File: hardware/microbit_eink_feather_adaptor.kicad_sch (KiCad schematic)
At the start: 2 parts

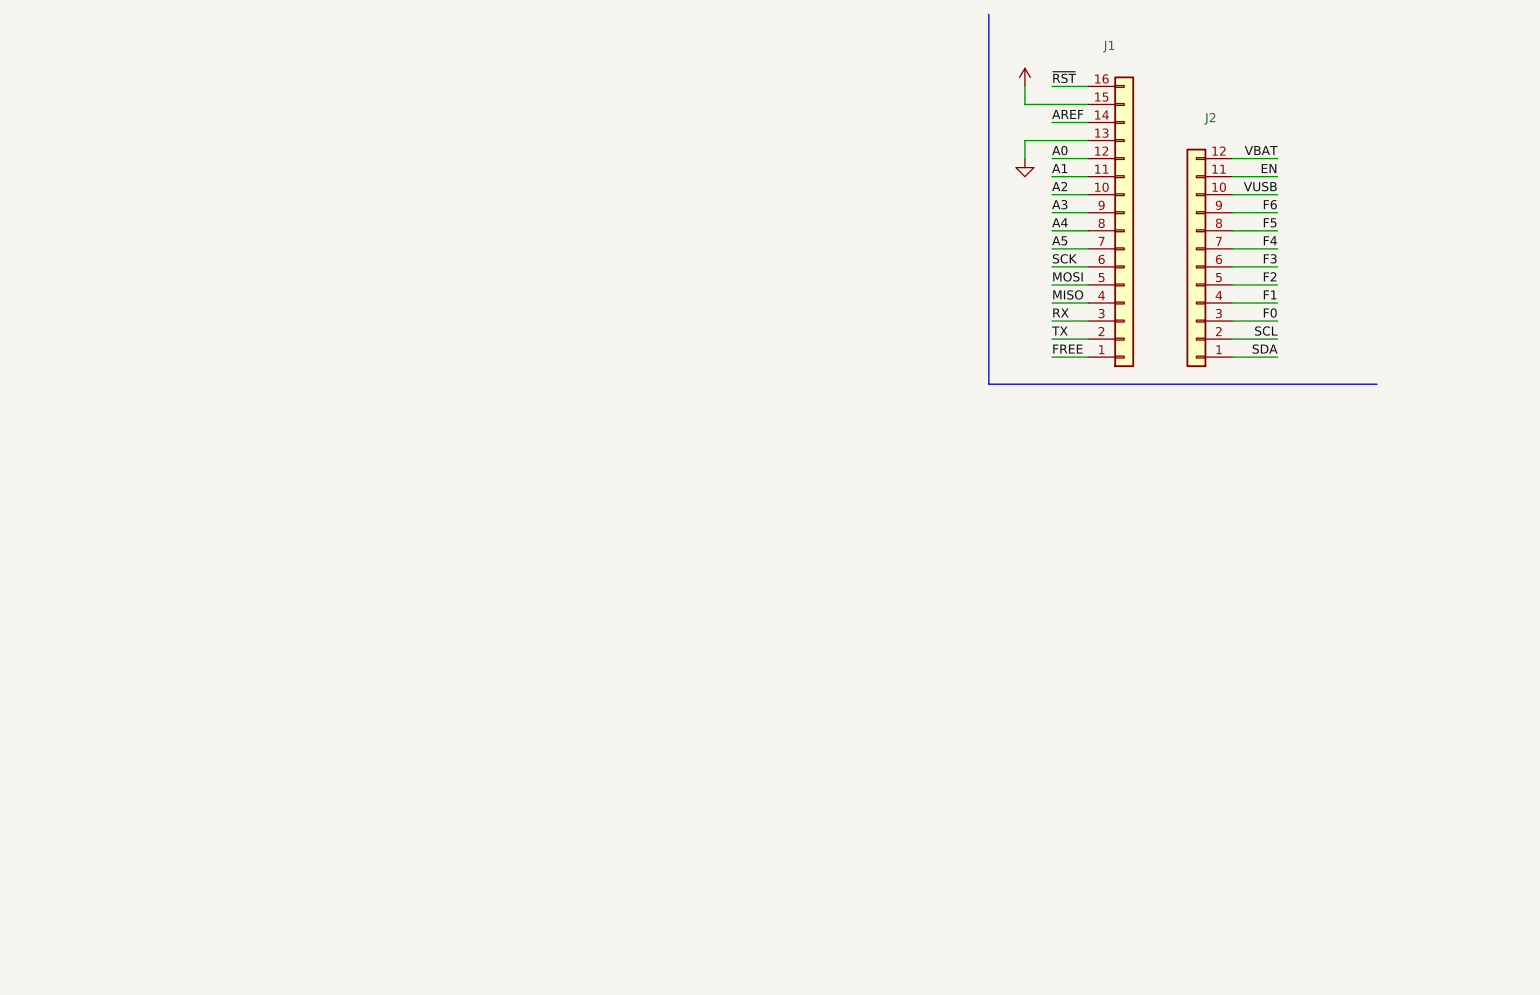
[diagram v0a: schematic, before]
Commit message: Add micro:bit edge connector to project.
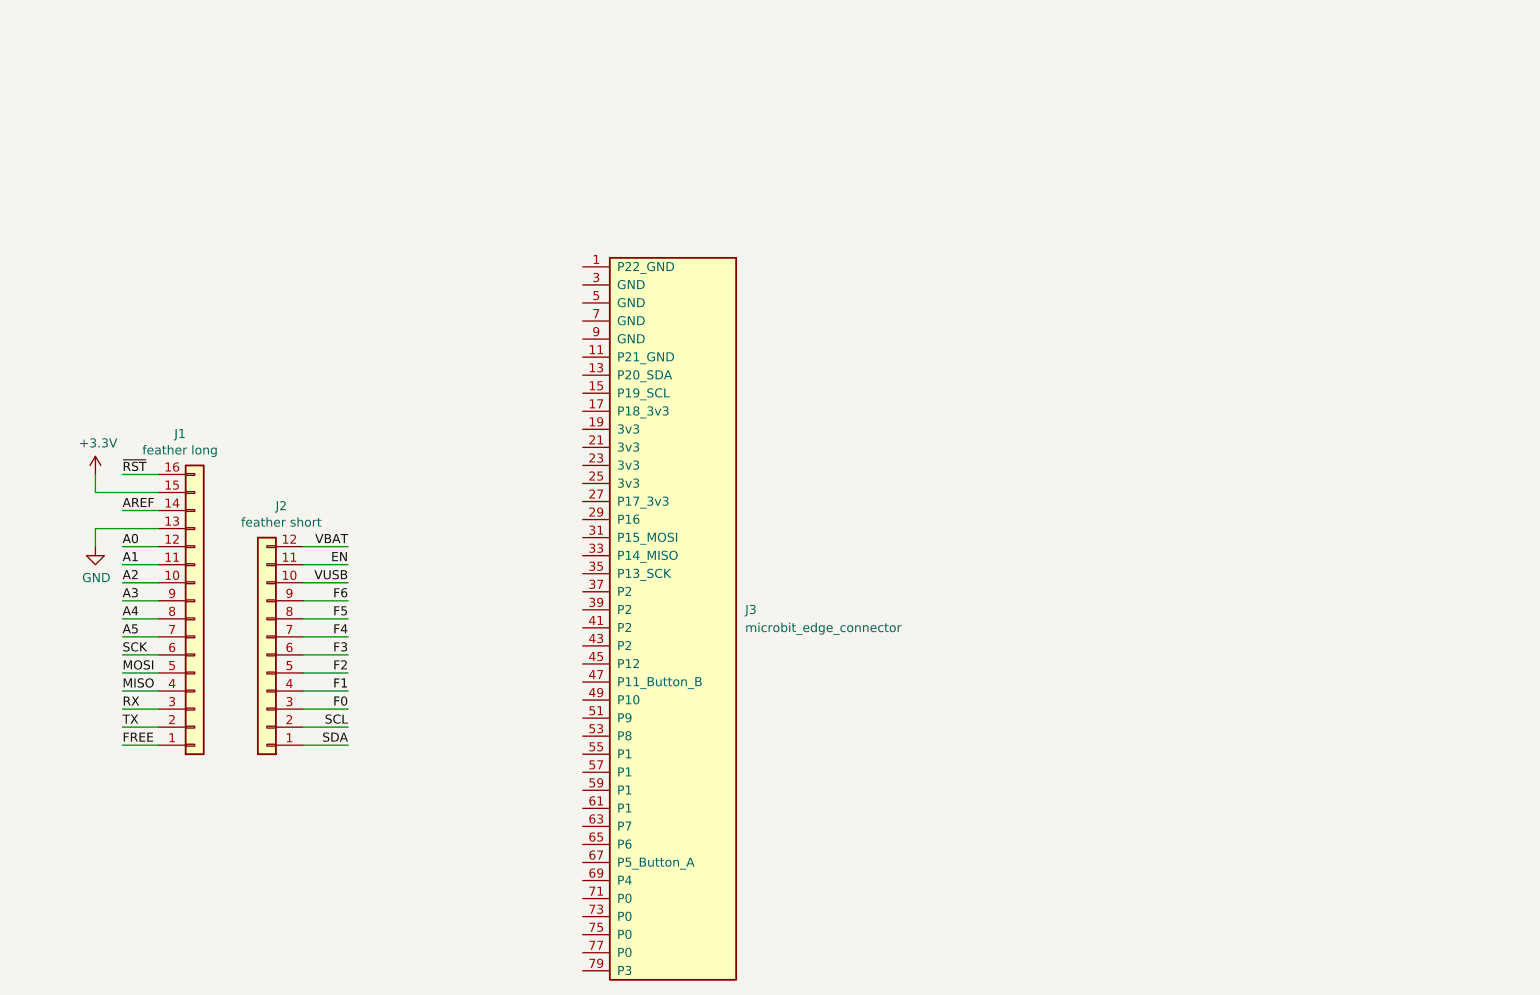
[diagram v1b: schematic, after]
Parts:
- added J3: microbit_edge_connector, symbol lib_microbit_connector:microbit_edge_connector
- J1: value (none) -> feather long; footprint (none) -> Connector_PinHeader_2.54mm:PinHeader_1x16_P2.54mm_Vertical
- J2: value (none) -> feather short; footprint (none) -> Connector_PinHeader_2.54mm:PinHeader_1x12_P2.54mm_Vertical
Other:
- moved on the sheet: J1, J2

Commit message: Increase board size, place edge connector, and route 3V, GND, and SPI pins.
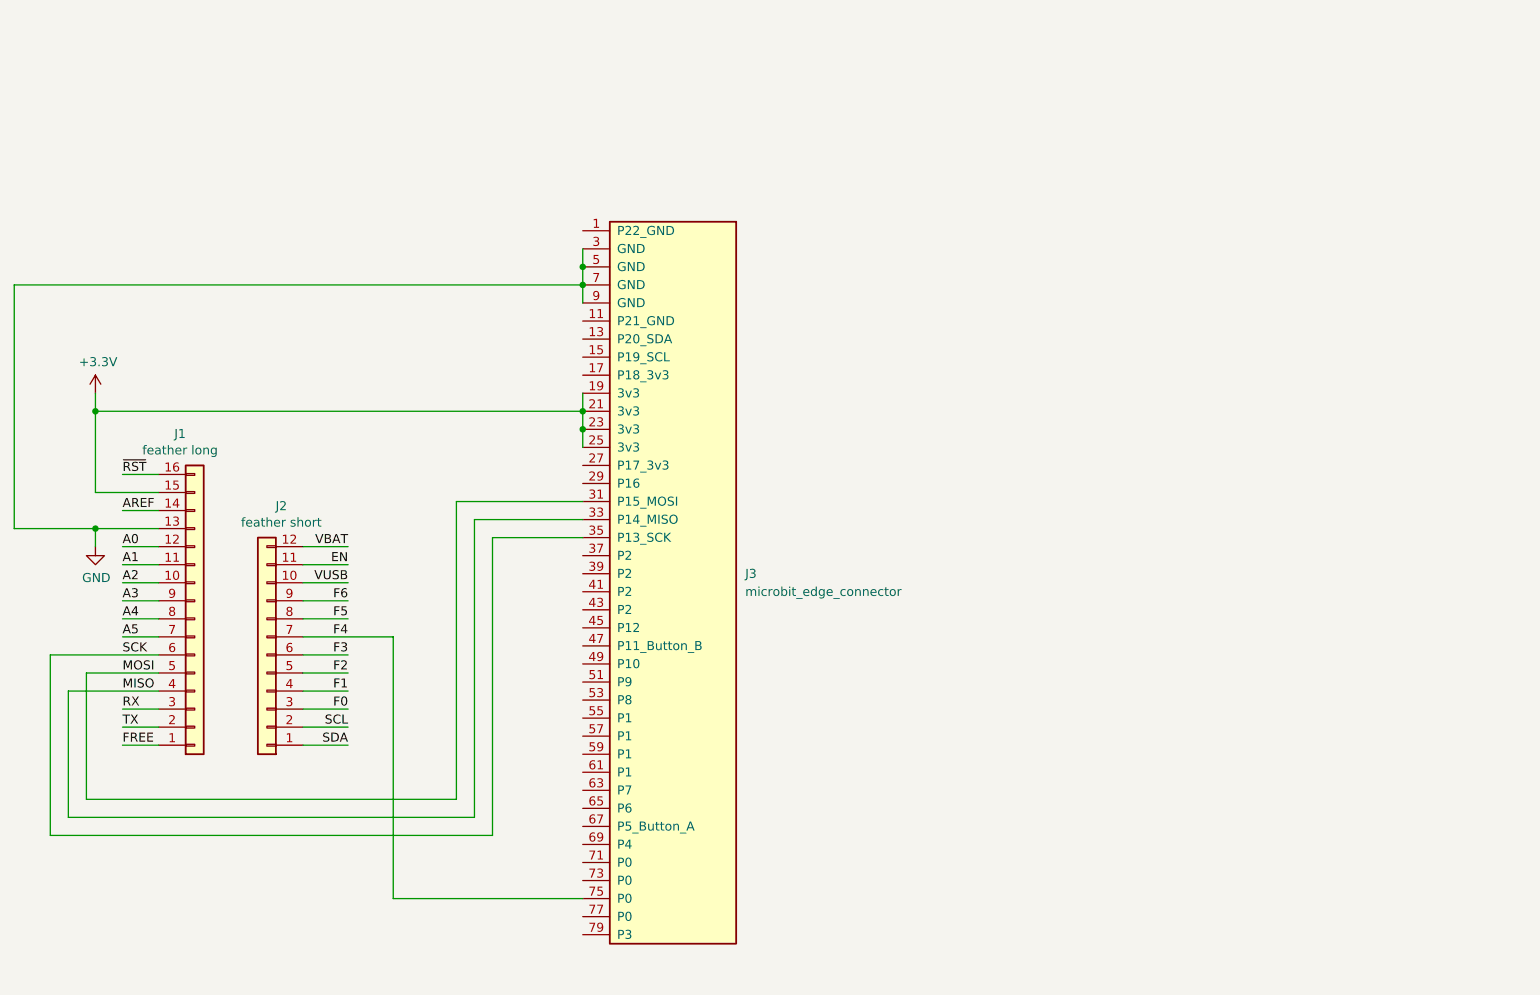
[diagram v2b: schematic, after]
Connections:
- net +3V3: now also J3.19 (3v3), J3.21 (3v3), J3.23 (3v3), J3.25 (3v3)
- net F4: now also J3.75 (P0)
- net GND: now also J3.3 (GND), J3.5 (GND), J3.7 (GND), J3.9 (GND)
- net MISO: now also J3.33 (P14_MISO)
- net MOSI: now also J3.31 (P15_MOSI)
- net SCK: now also J3.35 (P13_SCK)
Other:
- moved on the sheet: J3
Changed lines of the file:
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@@
 (kicad_sch (version 20211123) (generator eeschema)
   (paper "USLetter")
+  (junction (at 154.94 68.58) (diameter 0) (color 0 0 0 0)
+  )
+  (junction (at 154.94 48.26) (diameter 0) (color 0 0 0 0)
+  )
+  (junction (at 154.94 71.12) (diameter 0) (color 0 0 0 0)
+  )
+  (junction (at 154.94 50.8) (diameter 0) (color 0 0 0 0)
+  )
+  (junction (at 86.36 85.09) (diameter 0) (color 0 0 0 0)
+  )
+  (junction (at 86.36 68.58) (diameter 0) (color 0 0 0 0)
+  )
   (wire (pts (xy 90.17 82.55) (xy 95.25 82.55))
     (stroke (width 0) (type default) (color 0 0 0 0))
   )
-  (wire (pts (xy 90.17 102.87) (xy 95.25 102.87))
+  (wire (pts (xy 142.24 86.36) (xy 142.24 128.27))
+    (stroke (width 0) (type default) (color 0 0 0 0))
+  )
+  (wire (pts (xy 139.7 83.82) (xy 139.7 125.73))
+    (stroke (width 0) (type default) (color 0 0 0 0))
+  )
+  (wire (pts (xy 154.94 137.16) (xy 128.27 137.16))
     (stroke (width 0) (type default) (color 0 0 0 0))
   )
@@
     (stroke (width 0) (type default) (color 0 0 0 0))
   )
+  (wire (pts (xy 154.94 71.12) (xy 154.94 73.66))
+    (stroke (width 0) (type default) (color 0 0 0 0))
+  )
+  (wire (pts (xy 154.94 83.82) (xy 139.7 83.82))
+    (stroke (width 0) (type default) (color 0 0 0 0))
+  )
+  (wire (pts (xy 82.55 125.73) (xy 82.55 107.95))
+    (stroke (width 0) (type default) (color 0 0 0 0))
+  )
+  (wire (pts (xy 154.94 81.28) (xy 137.16 81.28))
+    (stroke (width 0) (type default) (color 0 0 0 0))
+  )
+  (wire (pts (xy 154.94 66.04) (xy 154.94 68.58))
+    (stroke (width 0) (type default) (color 0 0 0 0))
+  )
   (wire (pts (xy 115.57 102.87) (xy 121.92 102.87))
     (stroke (width 0) (type default) (color 0 0 0 0))
@@
     (stroke (width 0) (type default) (color 0 0 0 0))
   )
+  (wire (pts (xy 85.09 105.41) (xy 95.25 105.41))
+    (stroke (width 0) (type default) (color 0 0 0 0))
+  )
   (wire (pts (xy 90.17 115.57) (xy 95.25 115.57))
     (stroke (width 0) (type default) (color 0 0 0 0))
   )
+  (wire (pts (xy 86.36 68.58) (xy 154.94 68.58))
+    (stroke (width 0) (type default) (color 0 0 0 0))
+  )
   (wire (pts (xy 115.57 115.57) (xy 121.92 115.57))
     (stroke (width 0) (type default) (color 0 0 0 0))
   )
+  (wire (pts (xy 154.94 68.58) (xy 154.94 71.12))
+    (stroke (width 0) (type default) (color 0 0 0 0))
+  )
   (wire (pts (xy 90.17 113.03) (xy 95.25 113.03))
     (stroke (width 0) (type default) (color 0 0 0 0))
   )
+  (wire (pts (xy 137.16 123.19) (xy 85.09 123.19))
+    (stroke (width 0) (type default) (color 0 0 0 0))
+  )
   (wire (pts (xy 115.57 90.17) (xy 121.92 90.17))
     (stroke (width 0) (type default) (color 0 0 0 0))
@@
     (stroke (width 0) (type default) (color 0 0 0 0))
   )
-  (wire (pts (xy 90.17 105.41) (xy 95.25 105.41))
-    (stroke (width 0) (type default) (color 0 0 0 0))
-  )
   (wire (pts (xy 115.57 97.79) (xy 121.92 97.79))
     (stroke (width 0) (type default) (color 0 0 0 0))
   )
+  (wire (pts (xy 128.27 137.16) (xy 128.27 100.33))
+    (stroke (width 0) (type default) (color 0 0 0 0))
+  )
   (wire (pts (xy 86.36 87.63) (xy 86.36 85.09))
     (stroke (width 0) (type default) (color 0 0 0 0))
@@
     (stroke (width 0) (type default) (color 0 0 0 0))
   )
+  (wire (pts (xy 74.93 85.09) (xy 86.36 85.09))
+    (stroke (width 0) (type default) (color 0 0 0 0))
+  )
+  (wire (pts (xy 86.36 68.58) (xy 86.36 80.01))
+    (stroke (width 0) (type default) (color 0 0 0 0))
+  )
   (wire (pts (xy 115.57 113.03) (xy 121.92 113.03))
     (stroke (width 0) (type default) (color 0 0 0 0))
@@
     (stroke (width 0) (type default) (color 0 0 0 0))
   )
-  (wire (pts (xy 90.17 107.95) (xy 95.25 107.95))
+  (wire (pts (xy 82.55 107.95) (xy 95.25 107.95))
     (stroke (width 0) (type default) (color 0 0 0 0))
   )
@@
     (stroke (width 0) (type default) (color 0 0 0 0))
   )
+  (wire (pts (xy 80.01 128.27) (xy 80.01 102.87))
+    (stroke (width 0) (type default) (color 0 0 0 0))
+  )
+  (wire (pts (xy 85.09 123.19) (xy 85.09 105.41))
+    (stroke (width 0) (type default) (color 0 0 0 0))
+  )
+  (wire (pts (xy 142.24 128.27) (xy 80.01 128.27))
+    (stroke (width 0) (type default) (color 0 0 0 0))
+  )
   (wire (pts (xy 90.17 95.25) (xy 95.25 95.25))
     (stroke (width 0) (type default) (color 0 0 0 0))
   )
+  (wire (pts (xy 154.94 45.72) (xy 154.94 48.26))
+    (stroke (width 0) (type default) (color 0 0 0 0))
+  )
+  (wire (pts (xy 74.93 50.8) (xy 74.93 85.09))
+    (stroke (width 0) (type default) (color 0 0 0 0))
+  )
+  (wire (pts (xy 154.94 50.8) (xy 154.94 53.34))
+    (stroke (width 0) (type default) (color 0 0 0 0))
+  )
   (wire (pts (xy 86.36 85.09) (xy 95.25 85.09))
     (stroke (width 0) (type default) (color 0 0 0 0))
@@
     (stroke (width 0) (type default) (color 0 0 0 0))
   )
-  (wire (pts (xy 115.57 100.33) (xy 121.92 100.33))
+  (wire (pts (xy 139.7 125.73) (xy 82.55 125.73))
     (stroke (width 0) (type default) (color 0 0 0 0))
   )
@@
     (stroke (width 0) (type default) (color 0 0 0 0))
   )
-  (wire (pts (xy 86.36 77.47) (xy 86.36 80.01))
+  (wire (pts (xy 86.36 66.04) (xy 86.36 68.58))
+    (stroke (width 0) (type default) (color 0 0 0 0))
+  )
+  (wire (pts (xy 115.57 100.33) (xy 128.27 100.33))
+    (stroke (width 0) (type default) (color 0 0 0 0))
+  )
+  (wire (pts (xy 80.01 102.87) (xy 95.25 102.87))
     (stroke (width 0) (type default) (color 0 0 0 0))
   )
   (wire (pts (xy 115.57 95.25) (xy 121.92 95.25))
+    (stroke (width 0) (type default) (color 0 0 0 0))
+  )
+  (wire (pts (xy 154.94 48.26) (xy 154.94 50.8))
+    (stroke (width 0) (type default) (color 0 0 0 0))
+  )
+  (wire (pts (xy 137.16 81.28) (xy 137.16 123.19))
+    (stroke (width 0) (type default) (color 0 0 0 0))
+  )
+  (wire (pts (xy 154.94 86.36) (xy 142.24 86.36))
+    (stroke (width 0) (type default) (color 0 0 0 0))
+  )
+  (wire (pts (xy 154.94 50.8) (xy 74.93 50.8))
     (stroke (width 0) (type default) (color 0 0 0 0))
   )
@@
     (pin "9")
   )
-  (symbol (lib_id "power:+3.3V") (at 86.36 77.47 0) (unit 1)
+  (symbol (lib_id "power:+3.3V") (at 86.36 66.04 0) (unit 1)
     (in_bom yes) (on_board yes)
-    (property "Reference" "#PWR01" (id 0) (at 86.36 81.28 0)
-      (effects (font (size 1.27 1.27)) hide)
-    )
-    (property "Value" "+3.3V" (id 1) (at 86.741 73.0758 0))
-    (property "Footprint" "" (id 2) (at 86.36 77.47 0)
-      (effects (font (size 1.27 1.27)) hide)
-    )
-    (property "Datasheet" "" (id 3) (at 86.36 77.47 0)
+    (property "Reference" "#PWR01" (id 0) (at 86.36 69.85 0)
+      (effects (font (size 1.27 1.27)) hide)
+    )
+    (property "Value" "+3.3V" (id 1) (at 86.741 61.6458 0))
+    (property "Footprint" "" (id 2) (at 86.36 66.04 0)
+      (effects (font (size 1.27 1.27)) hide)
+    )
+    (property "Datasheet" "" (id 3) (at 86.36 66.04 0)
       (effects (font (size 1.27 1.27)) hide)
     )
@@
     (pin "1")
   )
-  (symbol (lib_id "lib_microbit_connector:microbit_edge_connector") (at 167.64 93.98 0) (mirror y) (unit 1)
+  (symbol (lib_id "lib_microbit_connector:microbit_edge_connector") (at 167.64 88.9 0) (mirror y) (unit 1)
     (in_bom yes) (on_board yes) (fields_autoplaced)
-    (property "Reference" "J3" (id 0) (at 177.8 96.5199 0)
+    (property "Reference" "J3" (id 0) (at 177.8 91.4399 0)
       (effects (font (size 1.27 1.27)) (justify right))
     )
-    (property "Value" "microbit_edge_connector" (id 1) (at 177.8 99.0599 0)
+    (property "Value" "microbit_edge_connector" (id 1) (at 177.8 93.9799 0)
       (effects (font (size 1.27 1.27)) (justify right))
     )
-    (property "Footprint" "" (id 2) (at 170.18 96.52 0)
-      (effects (font (size 1.27 1.27)) hide)
-    )
-    (property "Datasheet" "https://www.microbit.co.uk/device/pins" (id 3) (at 170.18 96.52 0)
-      (effects (font (size 1.27 1.27)) hide)
-    )
+    (property "Footprint" "" (id 2) (at 170.18 91.44 0)
+      (effects (font (size 1.27 1.27)) hide)
+    )
+    (property "Datasheet" "https://www.microbit.co.uk/device/pins" (id 3) (at 170.18 91.44 0)
+      (effects (font (size 1.27 1.27)) hide)
+    )

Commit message: Route all pins and complete initial version of board.
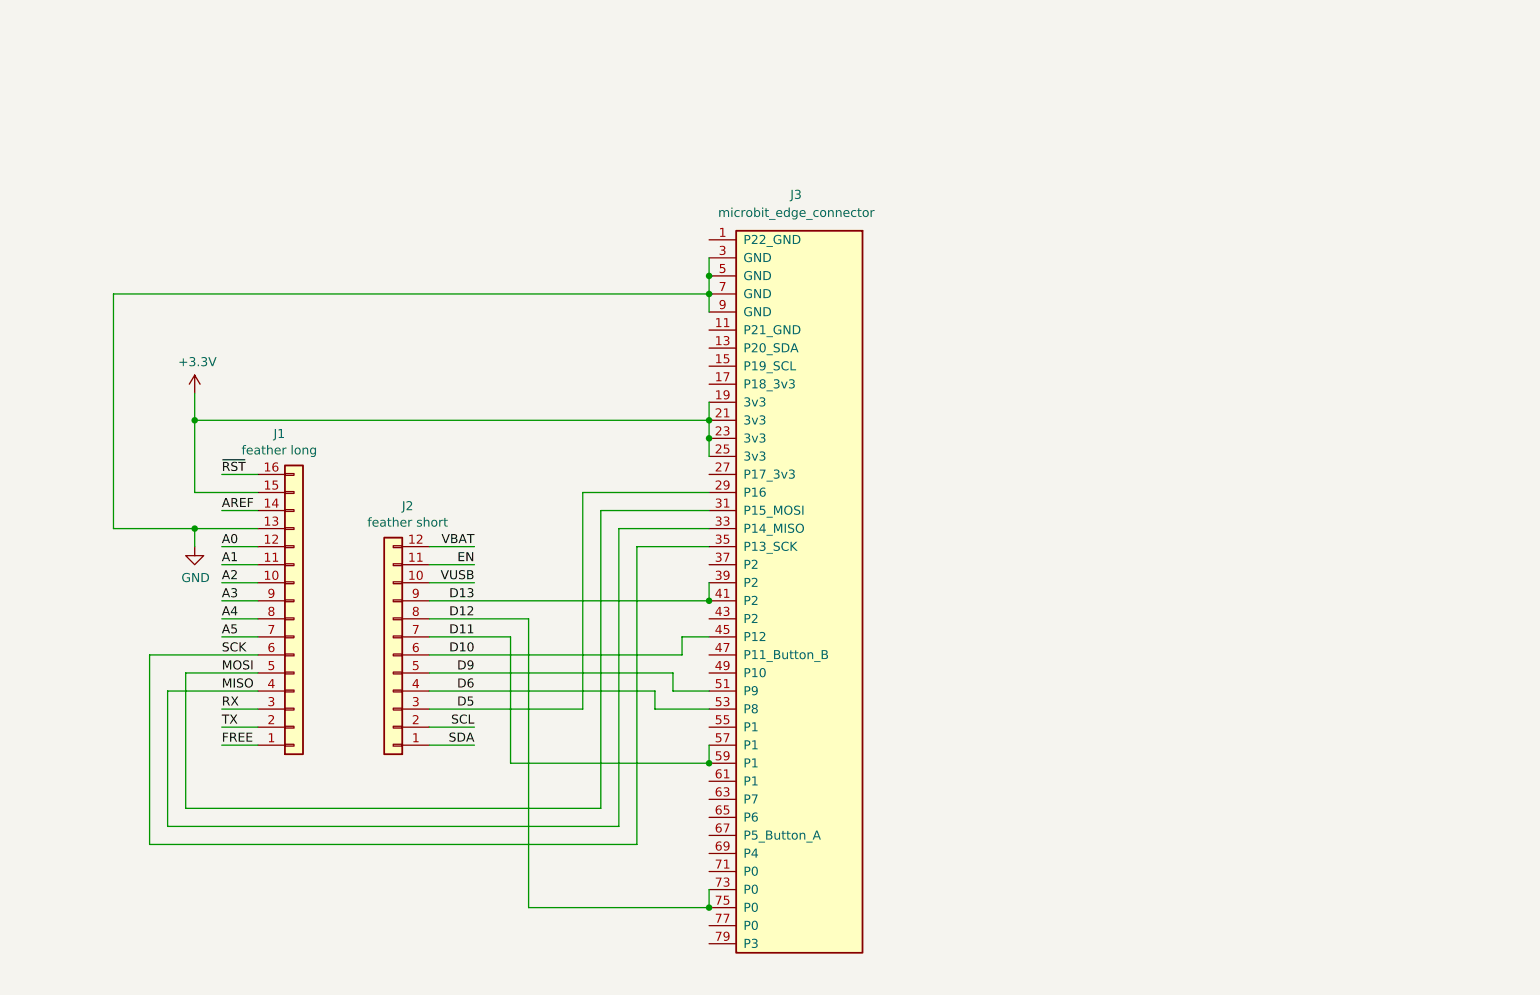
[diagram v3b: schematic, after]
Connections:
- net F0 is gone; now on net D5: J2.3 (Pin_3)
- net F1 is gone; now on net D6: J2.4 (Pin_4)
- net F2 is gone; now on net D9: J2.5 (Pin_5)
- net F3 is gone; now on net D10: J2.6 (Pin_6)
- net F5 is gone; now on net D12: J2.8 (Pin_8)
- net F6 is gone; now on net D13: J2.9 (Pin_9)
- net D5: now reaches J3.29 (P16)
- net D13: now reaches J3.39 (P2)
- net D13: now also J3.41 (P2)
- net D10: now reaches J3.45 (P12)
- net D9: now reaches J3.51 (P9)
- net D6: now reaches J3.53 (P8)
- net D11: now reaches J3.57 (P1)
- net D11: now also J2.7 (Pin_7), J3.59 (P1)
- net D12: now reaches J3.73 (P0)
- net D12: now also J3.75 (P0)
- removed net F4: J2.7 (Pin_7), J3.75 (P0)
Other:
- title: (none) -> micro:bit eInk FeatherWing Adaptor
- moved on the sheet: J1, J2, J3

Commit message: pcb: Expand PCB to include butterfly hang hole.
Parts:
- J3: footprint (none) -> Connector_PCBEdge:4UCON_10156_2x40_P1.27mm_Socket_Horizontal
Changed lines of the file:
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@@
   (title_block
     (title "micro:bit eInk FeatherWing Adaptor")
-    (date "2022-06-07")
-    (rev "V1.0")
+    (date "2022-06-26")
+    (rev "V1.1")
   )
   (junction (at 172.72 69.85) (diameter 0) (color 0 0 0 0)
@@
       (effects (font (size 1.27 1.27)) (justify right))
     )
-    (property "Footprint" "" (id 2) (at 187.96 92.71 0)
-      (effects (font (size 1.27 1.27)) hide)
-    )
+    (property "Footprint" "Connector_PCBEdge:4UCON_10156_2x40_P1.27mm_Socket_Horizontal" (id 2) (at 187.96 92.71 0)
+      (effects (font (size 1.27 1.27)) hide)
+    )
